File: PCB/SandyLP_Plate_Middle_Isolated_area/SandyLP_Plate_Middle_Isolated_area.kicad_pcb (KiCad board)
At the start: 2 copper layers, 42.3 x 20.8 mm, 5 parts

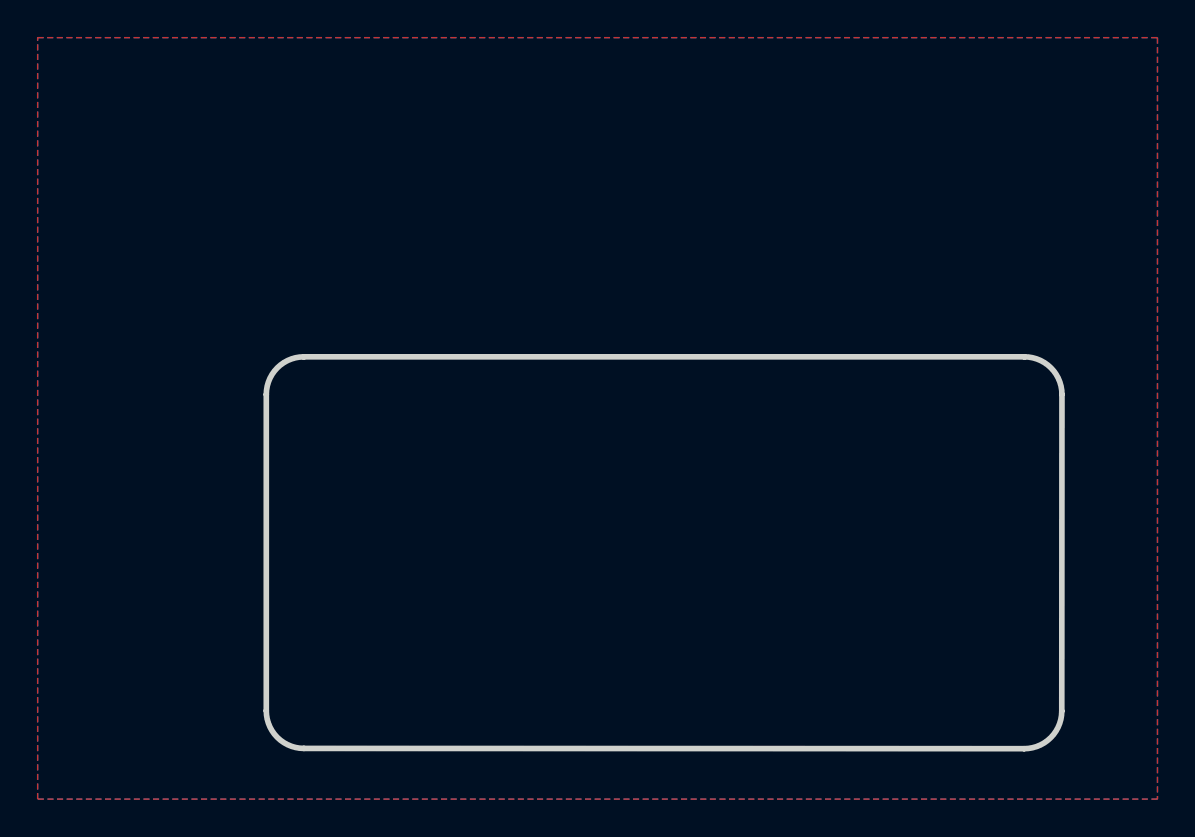
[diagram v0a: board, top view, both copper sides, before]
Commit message: 外形のコーナーを緩く。
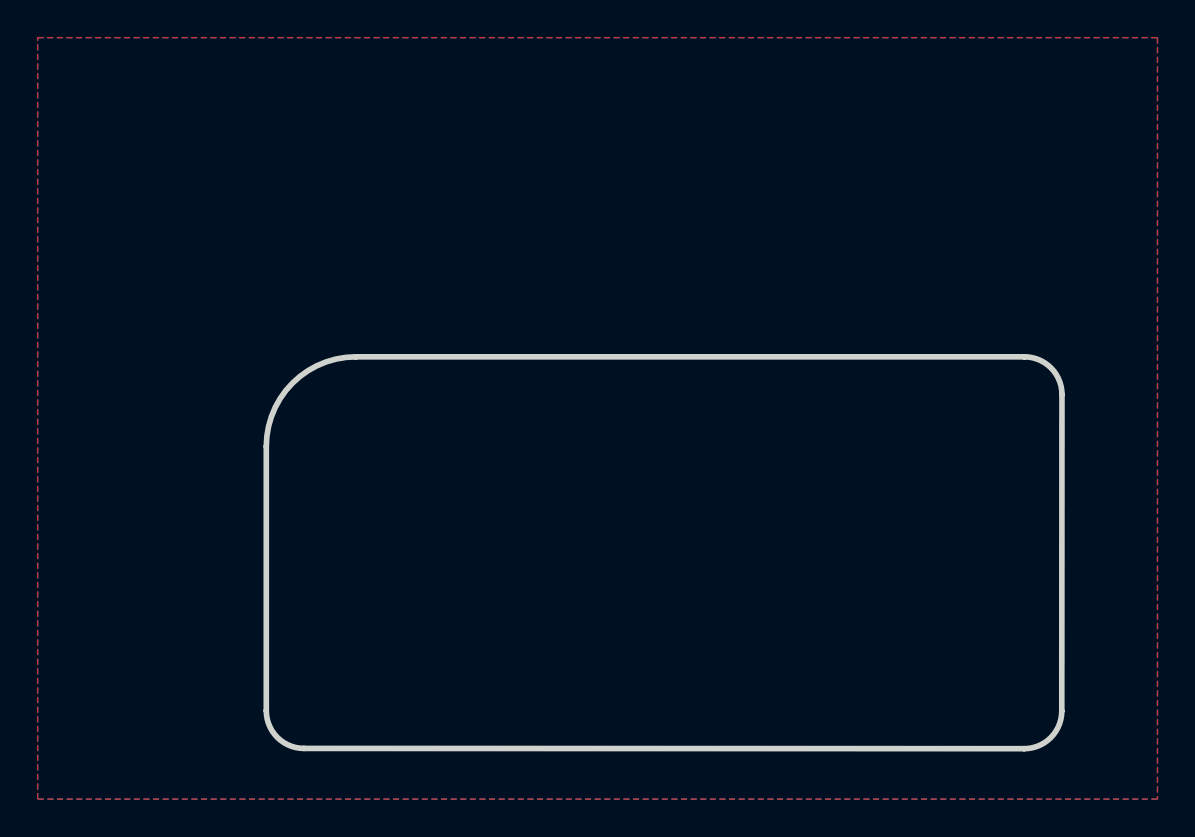
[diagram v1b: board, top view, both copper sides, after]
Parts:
- Cutout1: footprint locallib:SandyLP_outline_Mid_Isolated_Area -> locallib:SandyLP_outline_Mid_Isolated_Area_gentle_corner
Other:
- outline, holes or cut-outs redrawn
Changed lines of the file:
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@@
 	)
 	(net 0 "")
-	(footprint "locallib:SandyLP_outline_Mid_Isolated_Area"
+	(footprint "locallib:SandyLP_outline_Mid_Isolated_Area_gentle_corner"
 		(locked yes)
 		(layer "F.Cu")
@@
 			)
 		)
-		(property "Footprint" "locallib:SandyLP_outline_Mid_Isolated_Area"
+		(property "Footprint" "locallib:SandyLP_outline_Mid_Isolated_Area_gentle_corner"
 			(at 0 0 0)
 			(layer "F.Fab")
@@
 			)
 		)
-		(attr through_hole board_only)
+		(attr through_hole)
 		(fp_line
 			(start -47.625 -38.1)
@@
 		(fp_line
 			(start -42.6125 -2.314214)
-			(end -42.6125 -19.13129)
-			(stroke
-				(width 0.3)
-				(type solid)
-			)
-			(layer "Edge.Cuts")
-		)
-		(fp_line
-			(start -40.6125 -21.13129)
-			(end -2.315 -21.13129)
+			(end -42.6125 -16.36879)
 			(stroke
 				(width 0.3)
@@
 		)
 		(fp_line
+			(start -37.85 -21.13129)
+			(end -2.315 -21.13129)
+			(stroke
+				(width 0.3)
+				(type solid)
+			)
+			(layer "Edge.Cuts")
+		)
+		(fp_line
 			(start -0.325 -2.3)
 			(end -0.315 -19.13129)
@@
 		)
 		(fp_arc
-			(start -42.6125 -19.13129)
-			(mid -42.026714 -20.545504)
-			(end -40.6125 -21.13129)
-			(stroke
-				(width 0.3)
-				(type solid)
-			)
-			(layer "Edge.Cuts")
+			(start -42.6125 -16.36879)
+			(mid -41.217596 -19.736386)
+			(end -37.85 -21.13129)
+			(stroke
+				(width 0.3)
+				(type default)
+			)
+			(layer "Edge.Cuts")

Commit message: スイッチ穴をPTHに変更。
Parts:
- SW_BS1, SW_P1: footprint locallib:MX-Switch-Hole -> locallib:MXOnly-1U-Hotswap-guide-dummy
- SW_Q1, SW_TAB1: footprint locallib:MX-Switch-Hole -> locallib:MX-Switch-Hole-with-narrow-frame
